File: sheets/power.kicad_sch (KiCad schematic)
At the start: 36 parts, among them J2 USB_C_Receptacle_USB2.0_16P, SW3 SW_SPDT, SW4 SW_SPST, U2 USBLC6-2P6, U3 TPS54620RGYR, U4 AMS1117-3.3, U5 LMR51430XFDDCR

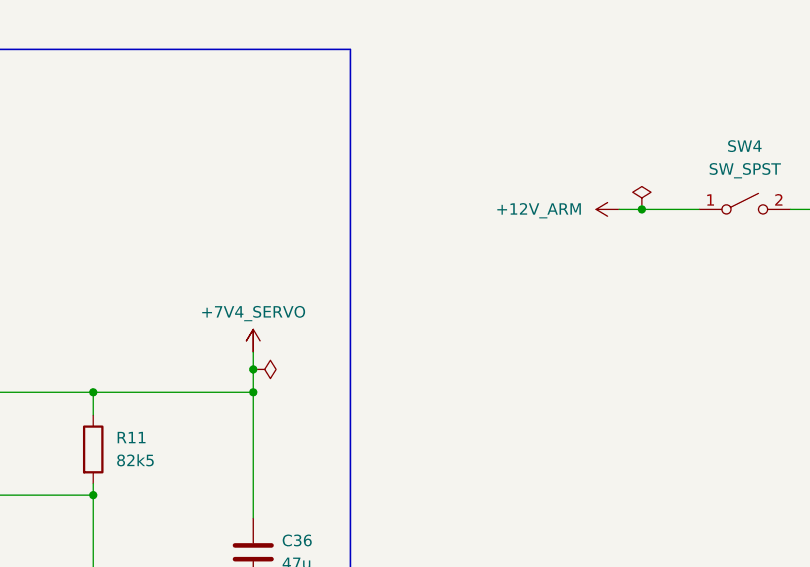
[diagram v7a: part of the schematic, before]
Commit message: Cleared ALL ERC warnings
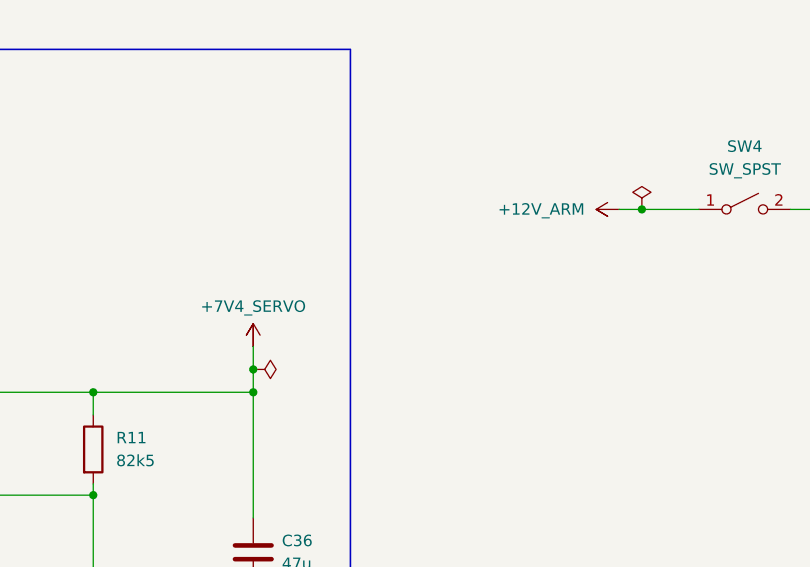
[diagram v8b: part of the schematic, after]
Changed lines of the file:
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@@
 	(wire
 		(pts
-			(xy 161.29 147.955) (xy 161.29 149.86)
+			(xy 161.29 147.32) (xy 161.29 149.86)
 		)
 		(stroke
@@
 	)
 	(symbol
-		(lib_id "Power:+12V_ARM")
-		(at 201.93 132.08 90)
-		(unit 1)
-		(exclude_from_sim no)
-		(in_bom no)
-		(on_board no)
-		(dnp no)
-		(property "Reference" "#PWR036"
-			(at 201.93 132.08 0)
-			(effects
-				(font
-					(size 1.27 1.27)
-				)
-				(hide yes)
-			)
-		)
-		(property "Value" "+12V_ARM"
-			(at 193.04 132.08 90)
-			(effects
-				(font
-					(size 1.27 1.27)
-				)
-			)
-		)
-		(property "Footprint" ""
-			(at 201.93 132.08 0)
-			(effects
-				(font
-					(size 1.27 1.27)
-				)
-				(hide yes)
-			)
-		)
-		(property "Datasheet" ""
-			(at 201.93 132.08 0)
-			(effects
-				(font
-					(size 1.27 1.27)
-				)
-				(hide yes)
-			)
-		)
-		(property "Description" "For ARMING ematches."
-			(at 201.93 132.08 0)
-			(effects
-				(font
-					(size 1.27 1.27)
-				)
-				(hide yes)
-			)
-		)
-		(pin ""
-		)
-		(instances
-			(project "aerolotl"
-				(path "/3f5bc5ea-feaa-4ed9-b0e0-c918b1fb5754/74cb3ba4-5441-4040-b144-f529fa281743"
-					(reference "#PWR036")
-					(unit 1)
-				)
-			)
-		)
-	)
-	(symbol
 		(lib_id "power:PWR_FLAG")
 		(at 204.47 132.08 0)
@@
 	)
 	(symbol
+		(lib_id "aerolotl_custom:+12V_ARM")
+		(at 201.93 132.08 90)
+		(unit 1)
+		(exclude_from_sim no)
+		(in_bom no)
+		(on_board no)
+		(dnp no)
+		(fields_autoplaced yes)
+		(property "Reference" "#PWR036"
+			(at 201.93 132.08 0)
+			(effects
+				(font
+					(size 1.27 1.27)
+				)
+				(hide yes)
+			)
+		)
+		(property "Value" "+12V_ARM"
+			(at 198.12 132.0799 90)
+			(effects
+				(font
+					(size 1.27 1.27)
+				)
+				(justify left)
+			)
+		)
+		(property "Footprint" ""
+			(at 201.93 132.08 0)
+			(effects
+				(font
+					(size 1.27 1.27)
+				)
+				(hide yes)
+			)
+		)
+		(property "Datasheet" ""
+			(at 201.93 132.08 0)
+			(effects
+				(font
+					(size 1.27 1.27)
+				)
+				(hide yes)
+			)
+		)
+		(property "Description" ""
+			(at 201.93 132.08 0)
+			(effects
+				(font
+					(size 1.27 1.27)
+				)
+				(hide yes)
+			)
+		)
+		(pin ""
+		)
+		(instances
+			(project ""
+				(path "/3f5bc5ea-feaa-4ed9-b0e0-c918b1fb5754/74cb3ba4-5441-4040-b144-f529fa281743"
+					(reference "#PWR036")
+					(unit 1)
+				)
+			)
+		)
+	)
+	(symbol
 		(lib_id "power:GND")
 		(at 246.38 144.78 0)
@@
 	(symbol
 		(lib_id "aerolotl_custom:+7V4_SERVO")
-		(at 161.29 147.955 0)
+		(at 161.29 147.32 0)
 		(unit 1)
 		(exclude_from_sim no)
@@
 		(fields_autoplaced yes)
 		(property "Reference" "#PWR034"
-			(at 161.29 147.955 0)
+			(at 161.29 147.32 0)
 			(effects
 				(font
@@
 		)
 		(property "Value" "+7V4_SERVO"
-			(at 161.29 143.51 0)
+			(at 161.29 142.875 0)
 			(effects
 				(font
@@
 		)
 		(property "Footprint" ""
-			(at 161.29 147.955 0)
+			(at 161.29 147.32 0)
 			(effects
 				(font
@@
 		)
 		(property "Datasheet" ""
-			(at 161.29 147.955 0)
+			(at 161.29 147.32 0)
 			(effects
 				(font
@@
 		)
 		(property "Description" ""
-			(at 161.29 147.955 0)
+			(at 161.29 147.32 0)
 			(effects
 				(font
